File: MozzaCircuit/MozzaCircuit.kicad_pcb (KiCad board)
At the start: 2 copper layers, 11 parts

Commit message: init pcb
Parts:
- removed C?: C_2012, 00_KeyParts:C_2012
- removed L? (x2): WS2812B, 00_KeyParts:WS2812B_2020_rev
- removed REF** (x3): ChocV2_rev, 00_KeyParts:ChocV2_rev
- removed REF** (x3): C_0603_1608Metric_Pad1.08x0.95mm_HandSolder, Capacitor_SMD:C_0603_1608Metric_Pad1.08x0.95mm_HandSolder
- removed REF**: D_SOD-323_HandSoldering, Diode_SMD:D_SOD-323_HandSoldering
- removed REF**: WS2812C-2020, 00_KeyParts:LED_WS2812C-2020_BackMount_v2
- added C1: 0.1u, 00_KeyParts:C_2012, F.Cu at (206.2, 46.5)
- added C11: 0.1u, 00_KeyParts:C_2012_rev, F.Cu at (59.6, 141.2)
- added C12: C_Small, 00_KeyParts:C_2012_rev, F.Cu at (74.7, 130.1)
- added C13: C_Small, 00_KeyParts:C_2012_rev, F.Cu at (64.3, 144.2)
- added C14: C_Small, 00_KeyParts:C_2012_rev, F.Cu at (64.8, 138.3)
- added C15: C_Small, 00_KeyParts:C_2012_rev, F.Cu at (54.8, 142.4)
- added C2: C_Small, 00_KeyParts:C_2012, F.Cu at (234.0, 28.9)
- added C21: C_Small, 00_KeyParts:C_2012_rev, F.Cu at (44.4, 151.8)
- added C22: C_Small, 00_KeyParts:C_2012_rev, F.Cu at (69.5, 134.2)
- added C23: C_Small, 00_KeyParts:C_2012_rev, F.Cu at (59.6, 144.2)
- added C24: C_Small, 00_KeyParts:C_2012_rev, F.Cu at (74.3, 136.0)
- added C25: C_Small, 00_KeyParts:C_2012_rev, F.Cu at (49.6, 150.7)
- added C31: C_Small, 00_KeyParts:C_2012_rev, F.Cu at (64.8, 135.3)
- added C32: C_Small, 00_KeyParts:C_2012_rev, F.Cu at (54.4, 148.3)
- added C33: C_Small, 00_KeyParts:C_2012_rev, F.Cu at (53.9, 154.2)
- added C34: C_Small, 00_KeyParts:C_2012_rev, F.Cu at (70.4, 127.1)
- added C35: C_Small, 00_KeyParts:C_2012_rev, F.Cu at (64.3, 141.2)
- added C41: C_Small, 00_KeyParts:C_2012_rev, F.Cu at (69.5, 140.1)
- added C42: C_Small, 00_KeyParts:C_2012_rev, F.Cu at (54.8, 139.5)
- added C43: C_Small, 00_KeyParts:C_2012_rev, F.Cu at (79.9, 127.1)
- added C44: C_Small, 00_KeyParts:C_2012_rev, F.Cu at (59.6, 147.1)
- added C51: C_Small, 00_KeyParts:C_2012_rev, F.Cu at (64.3, 147.1)
- added C52: C_Small, 00_KeyParts:C_2012_rev, F.Cu at (49.6, 147.7)
- added C53: C_Small, 00_KeyParts:C_2012_rev, F.Cu at (79.5, 130.1)
- added C54: C_Small, 00_KeyParts:C_2012_rev, F.Cu at (69.5, 137.1)
- added C61: C_Small, 00_KeyParts:C_2012_rev, F.Cu at (49.2, 153.6)
- added C62: C_Small, 00_KeyParts:C_2012_rev, F.Cu at (70.0, 131.2)
- added C63: C_Small, 00_KeyParts:C_2012_rev, F.Cu at (75.2, 127.1)
- added C64: C_Small, 00_KeyParts:C_2012_rev, F.Cu at (60.0, 135.3)
- added C71: C_Small, 00_KeyParts:C_2012_rev, F.Cu at (59.1, 150.1)
- added C72: C_Small, 00_KeyParts:C_2012_rev, F.Cu at (74.7, 133.0)
- added C73: C_Small, 00_KeyParts:C_2012_rev, F.Cu at (65.2, 131.2)
- added C82: C_Small, 00_KeyParts:C_2012_rev, F.Cu at (54.8, 145.4)
- added C83: C_Small, 00_KeyParts:C_2012_rev, F.Cu at (60.0, 138.3)
- added C84: C_Small, 00_KeyParts:C_2012_rev, F.Cu at (54.4, 151.3)
- added CA1: 33n, 00_KeyParts:C_2012_rev, F.Cu at (159.7, 58.7)
- added CB1: C_Small, 00_KeyParts:C_2012_rev, F.Cu at (178.2, 34.8)
- added CD1: 33n, 00_KeyParts:C_2012_rev, F.Cu at (174.6, 49.8)
- added CD2: C_Small, 00_KeyParts:C_2012_rev, F.Cu at (164.7, 52.8)
- added CD3: C_Small, 00_KeyParts:C_2012_rev, F.Cu at (183.0, 37.8)
- added CD4: C_Small, 00_KeyParts:C_2012_rev, F.Cu at (99.5, 118.7)
- added CD5: C_Small, 00_KeyParts:C_2012_rev, F.Cu at (178.2, 43.7)
- added CD6: C_Small, 00_KeyParts:C_2012_rev, F.Cu at (141.7, 76.6)
- added CD7: C_Small, 00_KeyParts:C_2012_rev, F.Cu at (159.7, 64.6)
- added CD8: C_Small, 00_KeyParts:C_2012_rev, F.Cu at (94.8, 118.7)
- added D12: D_Small, 00_KeyParts:D_SOD-323_both_sides, F.Cu at (141.9, 67.8)
- added D13: D_Small, 00_KeyParts:D_SOD-323_both_sides, F.Cu at (147.0, 67.8)
- added D15: D_Small, 00_KeyParts:D_SOD-323_both_sides, F.Cu at (64.6, 118.7)
- added D21: D_Small, 00_KeyParts:D_SOD-323_both_sides, F.Cu at (89.9, 118.7)
- added D22: D_Small, 00_KeyParts:D_SOD-323_both_sides, F.Cu at (39.3, 118.7)
- added D23: D_Small, 00_KeyParts:D_SOD-323_both_sides, F.Cu at (170.0, 46.9)
- added D24: D_Small, 00_KeyParts:D_SOD-323_both_sides, F.Cu at (59.5, 118.7)
- added D25: D_Small, 00_KeyParts:D_SOD-323_both_sides, F.Cu at (69.6, 118.7)
- added D31: D_Small, 00_KeyParts:D_SOD-323_both_sides, F.Cu at (164.9, 46.9)
- added D32: D_Small, 00_KeyParts:D_SOD-323_both_sides, F.Cu at (44.3, 116.8)
- added D33: D_Small, 00_KeyParts:D_SOD-323_both_sides, F.Cu at (159.9, 46.9)
- added D34: D_Small, 00_KeyParts:D_SOD-323_both_sides, F.Cu at (147.0, 64.8)
- added D35: D_Small, 00_KeyParts:D_SOD-323_both_sides, F.Cu at (159.9, 49.8)
- added D41: D_Small, 00_KeyParts:D_SOD-323_both_sides, F.Cu at (178.4, 31.9)
- added D42: D_Small, 00_KeyParts:D_SOD-323_both_sides, F.Cu at (74.7, 118.7)
- added D43: D_Small, 00_KeyParts:D_SOD-323_both_sides, F.Cu at (164.9, 49.8)
- added D44: D_Small, 00_KeyParts:D_SOD-323_both_sides, F.Cu at (141.9, 70.7)
- added D45: D_Small, 00_KeyParts:D_SOD-323_both_sides, F.Cu at (152.0, 64.8)
- added D51: D_Small, 00_KeyParts:D_SOD-323_both_sides, F.Cu at (159.9, 55.7)
- added D52: D_Small, 00_KeyParts:D_SOD-323_both_sides, F.Cu at (34.2, 119.7)
- added D53: D_Small, 00_KeyParts:D_SOD-323_both_sides, F.Cu at (44.3, 119.7)
- added D54: D_Small, 00_KeyParts:D_SOD-323_both_sides, F.Cu at (159.9, 52.8)
- added D61: D_Small, 00_KeyParts:D_SOD-323_both_sides, F.Cu at (183.5, 28.9)
- added D62: D_Small, 00_KeyParts:D_SOD-323_both_sides, F.Cu at (141.9, 73.7)
- added D63: D_Small, 00_KeyParts:D_SOD-323_both_sides, F.Cu at (79.7, 118.7)
- added D64: D_Small, 00_KeyParts:D_SOD-323_both_sides, F.Cu at (178.4, 28.9)
- added D71: D_Small, 00_KeyParts:D_SOD-323_both_sides, F.Cu at (141.9, 64.8)
- added D72: D_Small, 00_KeyParts:D_SOD-323_both_sides, F.Cu at (54.4, 118.7)
- added D73: D_Small, 00_KeyParts:D_SOD-323_both_sides, F.Cu at (34.2, 116.8)
- added D82: D_Small, 00_KeyParts:D_SOD-323_both_sides, F.Cu at (84.8, 118.7)
- added D83: D_Small, 00_KeyParts:D_SOD-323_both_sides, F.Cu at (49.4, 118.7)
- added D84: D_Small, 00_KeyParts:D_SOD-323_both_sides, F.Cu at (124.0, 100.7)
- added J1: 8P8C_both_sides, 00_KeyParts:RJ45_Molex_0955032884_both_sides, F.Cu at (213.4, 30.0)
- added JPB2: SolderJumper_2_Open, Jumper:SolderJumper-2_P1.3mm_Open_TrianglePad1.0x1.5mm, F.Cu at (238.2, 32.8)
- added JPB3: SolderJumper_2_Open, Jumper:SolderJumper-2_P1.3mm_Open_TrianglePad1.0x1.5mm, F.Cu at (242.5, 32.8)
- added JPB4: SolderJumper_2_Open, Jumper:SolderJumper-2_P1.3mm_Open_TrianglePad1.0x1.5mm, F.Cu at (233.8, 32.2)
- added JPB6: SolderJumper_2_Open, Jumper:SolderJumper-2_P1.3mm_Open_TrianglePad1.0x1.5mm, F.Cu at (242.9, 29.2)
- added JPB7: SolderJumper_2_Open, Jumper:SolderJumper-2_P1.3mm_Open_TrianglePad1.0x1.5mm, F.Cu at (225.1, 46.7)
- added JPB8: SolderJumper_2_Open, Jumper:SolderJumper-2_P1.3mm_Open_TrianglePad1.0x1.5mm, F.Cu at (238.6, 29.2)
- added JPF2: SolderJumper_2_Open, Jumper:SolderJumper-2_P1.3mm_Open_TrianglePad1.0x1.5mm, F.Cu at (233.8, 39.3)
- added JPF3: SolderJumper_2_Open, Jumper:SolderJumper-2_P1.3mm_Open_TrianglePad1.0x1.5mm, F.Cu at (215.1, 46.8)
- added JPF4: SolderJumper_2_Open, Jumper:SolderJumper-2_P1.3mm_Open_TrianglePad1.0x1.5mm, F.Cu at (238.2, 36.3)
- added JPF6: SolderJumper_2_Open, Jumper:SolderJumper-2_P1.3mm_Open_TrianglePad1.0x1.5mm, F.Cu at (233.8, 35.7)
- added JPF7: SolderJumper_2_Open, Jumper:SolderJumper-2_P1.3mm_Open_TrianglePad1.0x1.5mm, F.Cu at (210.8, 46.8)
- added JPF8: SolderJumper_2_Open, Jumper:SolderJumper-2_P1.3mm_Open_TrianglePad1.0x1.5mm, F.Cu at (219.5, 46.8)
- added L12: WS2812-2020_both_sides, 00_KeyParts:WS2812B_2020_rev, F.Cu at (55.1, 135.9)
- added L13: WS2812-2020_both_sides, 00_KeyParts:WS2812B_2020_rev, F.Cu at (44.7, 144.2)
- added L15: WS2812-2020_both_sides, 00_KeyParts:WS2812B_2020_rev, F.Cu at (44.7, 131.8)
- added L21: WS2812-2020_both_sides, 00_KeyParts:WS2812B_2020_rev, F.Cu at (49.9, 140.0)
- added L22: WS2812-2020_both_sides, 00_KeyParts:WS2812B_2020_rev, F.Cu at (60.3, 131.8)
- added L23: WS2812-2020_both_sides, 00_KeyParts:WS2812B_2020_rev, F.Cu at (39.5, 148.3)
- added L24: WS2812-2020_both_sides, 00_KeyParts:WS2812B_2020_rev, F.Cu at (44.7, 127.7)
- added L25: WS2812-2020_both_sides, 00_KeyParts:WS2812B_2020_rev, F.Cu at (60.3, 127.7)
- added L31: WS2812-2020_both_sides, 00_KeyParts:WS2812B_2020_rev, F.Cu at (44.7, 148.3)
- added L32: WS2812-2020_both_sides, 00_KeyParts:WS2812B_2020_rev, F.Cu at (49.9, 131.8)
- added L33: WS2812-2020_both_sides, 00_KeyParts:WS2812B_2020_rev, F.Cu at (39.5, 144.2)
- added L34: WS2812-2020_both_sides, 00_KeyParts:WS2812B_2020_rev, F.Cu at (34.3, 127.7)
- added L35: WS2812-2020_both_sides, 00_KeyParts:WS2812B_2020_rev, F.Cu at (39.5, 135.9)
- added L41: WS2812-2020_both_sides, 00_KeyParts:WS2812B_2020_rev, F.Cu at (39.5, 140.0)
- added L42: WS2812-2020_both_sides, 00_KeyParts:WS2812B_2020_rev, F.Cu at (65.5, 127.7)
- added L43: WS2812-2020_both_sides, 00_KeyParts:WS2812B_2020_rev, F.Cu at (39.5, 131.8)
- added L44: WS2812-2020_both_sides, 00_KeyParts:WS2812B_2020_rev, F.Cu at (49.9, 135.9)
- added L51: WS2812-2020_both_sides, 00_KeyParts:WS2812B_2020_rev, F.Cu at (34.3, 140.0)
- added L52: WS2812-2020_both_sides, 00_KeyParts:WS2812B_2020_rev, F.Cu at (55.1, 131.8)
- added L53: WS2812-2020_both_sides, 00_KeyParts:WS2812B_2020_rev, F.Cu at (39.5, 152.4)
- added L54: WS2812-2020_both_sides, 00_KeyParts:WS2812B_2020_rev, F.Cu at (39.5, 127.7)
- added L61: WS2812-2020_both_sides, 00_KeyParts:WS2812B_2020_rev, F.Cu at (34.3, 152.4)
- added L62: WS2812-2020_both_sides, 00_KeyParts:WS2812B_2020_rev, F.Cu at (34.3, 135.9)
- added L63: WS2812-2020_both_sides, 00_KeyParts:WS2812B_2020_rev, F.Cu at (44.7, 140.0)
- added L64: WS2812-2020_both_sides, 00_KeyParts:WS2812B_2020_rev, F.Cu at (49.9, 144.2)
- added L71: WS2812-2020_both_sides, 00_KeyParts:WS2812B_2020_rev, F.Cu at (49.9, 127.7)
- added L72: WS2812-2020_both_sides, 00_KeyParts:WS2812B_2020_rev, F.Cu at (34.3, 148.3)
- added L73: WS2812-2020_both_sides, 00_KeyParts:WS2812B_2020_rev, F.Cu at (55.1, 127.7)
- added L82: WS2812-2020_both_sides, 00_KeyParts:WS2812B_2020_rev, F.Cu at (34.3, 144.2)
- added L83: WS2812-2020_both_sides, 00_KeyParts:WS2812B_2020_rev, F.Cu at (34.3, 131.8)
- added L84: WS2812-2020_both_sides, 00_KeyParts:WS2812B_2020_rev, F.Cu at (44.7, 135.9)
- added R11: 10k, 00_KeyParts:R_2012_rev, F.Cu at (104.3, 118.7)
- added R12: 4k7, 00_KeyParts:R_2012_rev, F.Cu at (188.0, 31.9)
- added R21: R_Small_US, 00_KeyParts:R_2012_rev, F.Cu at (146.8, 73.7)
- added R22: R_Small_US, 00_KeyParts:R_2012_rev, F.Cu at (146.8, 70.7)
- added R31: R_Small_US, 00_KeyParts:R_2012_rev, F.Cu at (169.8, 49.8)
- added R32: R_Small_US, 00_KeyParts:R_2012_rev, F.Cu at (188.4, 28.9)
- added R41: R_Small_US, 00_KeyParts:R_2012_rev, F.Cu at (159.7, 61.6)
- added R42: R_Small_US, 00_KeyParts:R_2012_rev, F.Cu at (178.2, 37.8)
- added R51: R_Small_US, 00_KeyParts:R_2012_rev, F.Cu at (183.3, 31.9)
- added R52: R_Small_US, 00_KeyParts:R_2012_rev, F.Cu at (164.7, 55.7)
- added R61: R_Small_US, 00_KeyParts:R_2012_rev, F.Cu at (164.4, 58.7)
- added R62: R_Small_US, 00_KeyParts:R_2012_rev, F.Cu at (183.0, 34.8)
- added R71: R_Small_US, 00_KeyParts:R_2012_rev, F.Cu at (146.5, 76.6)
- added R72: R_Small_US, 00_KeyParts:R_2012_rev, F.Cu at (151.5, 70.7)
- added R81: R_Small_US, 00_KeyParts:R_2012_rev, F.Cu at (174.9, 46.9)
- added R82: R_Small_US, 00_KeyParts:R_2012_rev, F.Cu at (169.5, 52.8)
- added RA1: 10k, 00_KeyParts:R_2012_rev, F.Cu at (187.7, 34.8)
- added RA2: 4k7, 00_KeyParts:R_2012_rev, F.Cu at (178.2, 40.7)
- added RB1: R_Small_US, 00_KeyParts:R_2012_rev, F.Cu at (193.1, 28.9)
- added RB2: R_Small_US, 00_KeyParts:R_2012_rev, F.Cu at (183.0, 40.7)
- added RE1: RotaryEncoder_Switch, 00_KeyParts:RotaryEncoder_Bourns_PEC12R-4215F, F.Cu at (41.2, 35.5)
- added SW12: SW_ChocV2_rev, 00_KeyParts:ChocV2_rev, F.Cu at (113.0, 36.4)
- added SW13: SW_ChocV2_rev, 00_KeyParts:ChocV2_rev, F.Cu at (76.5, 108.2)
- added SW15: SW_ChocV2_rev, 00_KeyParts:ChocV2_rev, F.Cu at (40.6, 106.3)
- added SW21: SW_ChocV2_rev, 00_KeyParts:ChocV2_rev, F.Cu at (58.6, 72.3)
- added SW22: SW_ChocV2_rev, 00_KeyParts:ChocV2_rev, F.Cu at (59.2, 36.4)
- added SW23: SW_ChocV2_rev, 00_KeyParts:ChocV2_rev, F.Cu at (130.4, 72.3)
- added SW24: SW_ChocV2_rev, 00_KeyParts:ChocV2_rev, F.Cu at (40.6, 52.5)
- added SW25: SW_ChocV2_rev, 00_KeyParts:ChocV2_rev, F.Cu at (77.1, 36.4)
- added SW31: SW_ChocV2_rev, 00_KeyParts:ChocV2_rev, F.Cu at (148.9, 36.4)
- added SW32: SW_ChocV2_rev, 00_KeyParts:ChocV2_rev, F.Cu at (112.4, 72.3)
- added SW33: SW_ChocV2_rev, 00_KeyParts:ChocV2_rev, F.Cu at (76.5, 90.3)
- added SW34: SW_ChocV2_rev, 00_KeyParts:ChocV2_rev, F.Cu at (112.4, 54.4)
- added SW35: SW_ChocV2_rev, 00_KeyParts:ChocV2_rev, F.Cu at (94.5, 72.3)
- added SW41: SW_ChocV2_rev, 00_KeyParts:ChocV2_rev, F.Cu at (166.9, 36.4)
- added SW42: SW_ChocV2_rev, 00_KeyParts:ChocV2_rev, F.Cu at (40.6, 70.4)
- added SW43: SW_ChocV2_rev, 00_KeyParts:ChocV2_rev, F.Cu at (130.4, 90.3)
- added SW44: SW_ChocV2_rev, 00_KeyParts:ChocV2_rev, F.Cu at (94.5, 90.3)
- added SW51: SW_ChocV2_rev, 00_KeyParts:ChocV2_rev, F.Cu at (76.5, 54.4)
- added SW52: SW_ChocV2_rev, 00_KeyParts:ChocV2_rev, F.Cu at (131.0, 36.4)
- added SW53: SW_ChocV2_rev, 00_KeyParts:ChocV2_rev, F.Cu at (130.4, 54.4)
- added SW54: SW_ChocV2_rev, 00_KeyParts:ChocV2_rev, F.Cu at (94.5, 54.4)
- added SW61: SW_ChocV2_rev, 00_KeyParts:ChocV2_rev, F.Cu at (58.6, 108.2)
- added SW62: SW_ChocV2_rev, 00_KeyParts:ChocV2_rev, F.Cu at (76.5, 72.3)
- added SW63: SW_ChocV2_rev, 00_KeyParts:ChocV2_rev, F.Cu at (94.5, 108.2)
- added SW64: SW_ChocV2_rev, 00_KeyParts:ChocV2_rev, F.Cu at (58.6, 90.3)
- added SW71: SW_ChocV2_rev, 00_KeyParts:ChocV2_rev, F.Cu at (95.1, 36.4)
- added SW72: SW_ChocV2_rev, 00_KeyParts:ChocV2_rev, F.Cu at (40.6, 88.4)
- added SW73: SW_ChocV2_rev, 00_KeyParts:ChocV2_rev, F.Cu at (148.3, 54.4)
- added SW82: SW_ChocV2_rev, 00_KeyParts:ChocV2_rev, F.Cu at (58.6, 54.4)
- added SW83: SW_ChocV2_rev, 00_KeyParts:ChocV2_rev, F.Cu at (112.4, 90.3)
- added SW84: SW_ChocV2_rev, 00_KeyParts:ChocV2_rev, F.Cu at (112.4, 108.2)
- added U1: MCP23017_ML, 00_KeyParts:QFN-28-1EP_6x6mm_P0.65mm_EP4.25x4.25mm_Hand, F.Cu at (227.3, 40.6)
- added U2: MCP23017_ML, 00_KeyParts:QFN-28-1EP_6x6mm_P0.65mm_EP4.25x4.25mm_Hand_NoTP, F.Cu at (227.3, 31.8)
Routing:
- net (no net): track 96.9 -> 0.00 mm, vias 8 -> 0

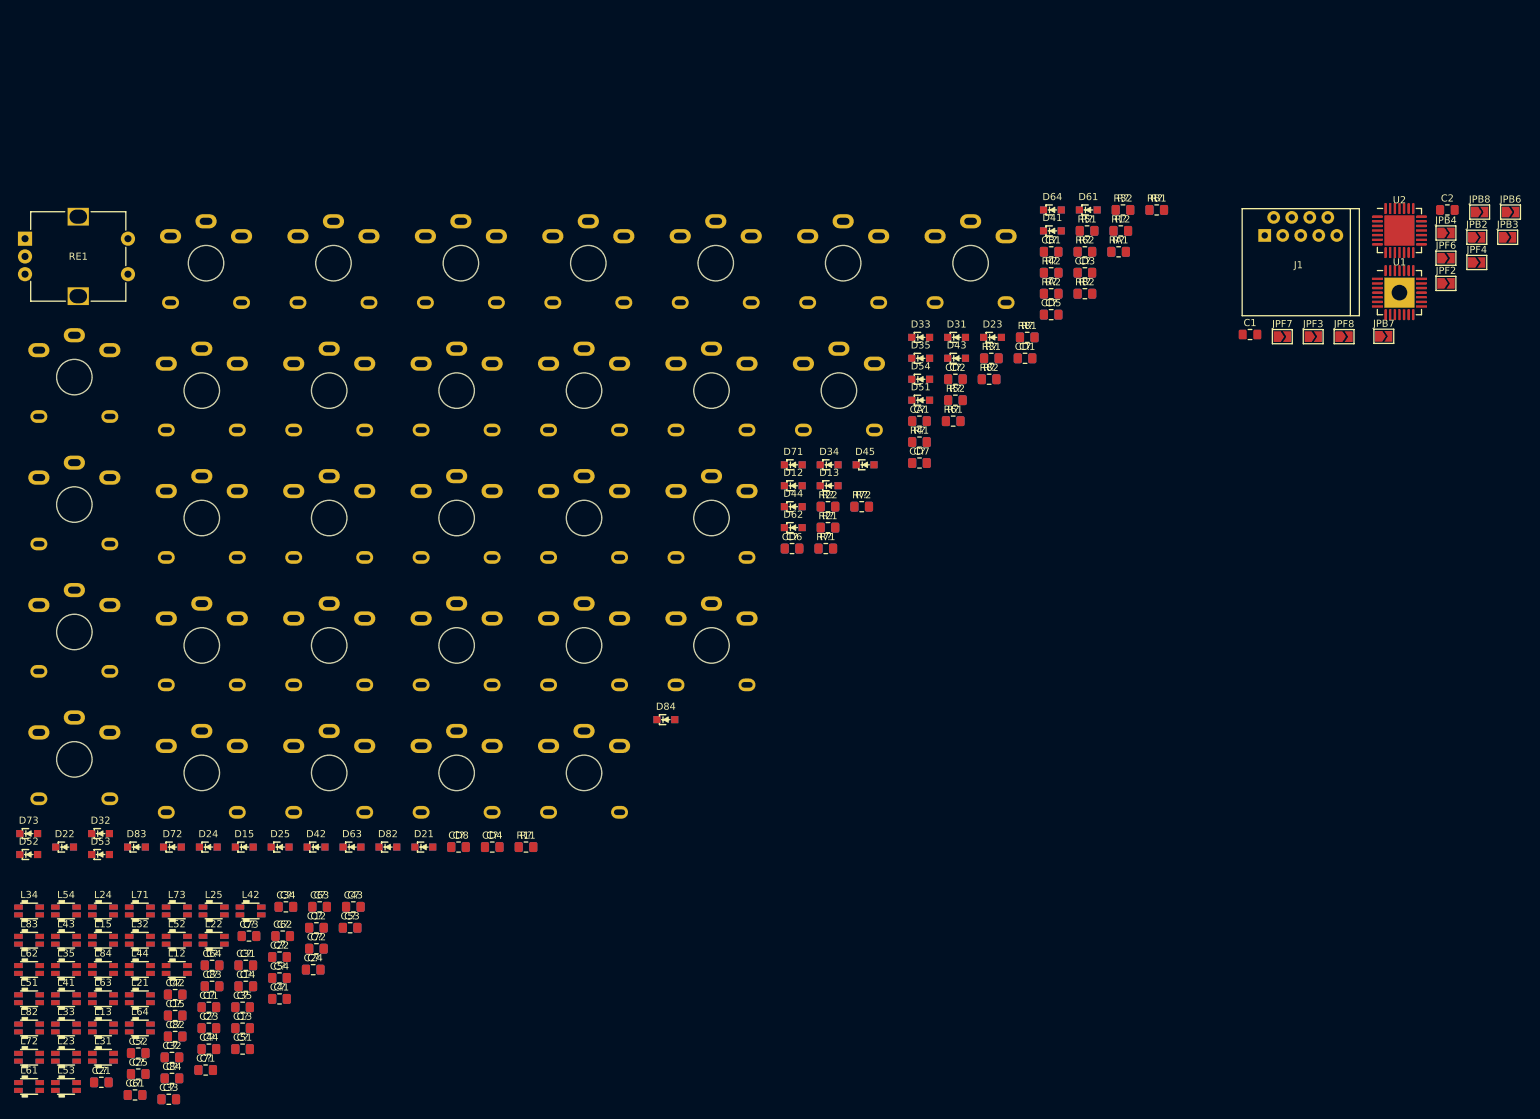
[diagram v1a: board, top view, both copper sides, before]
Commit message: placed sw and led
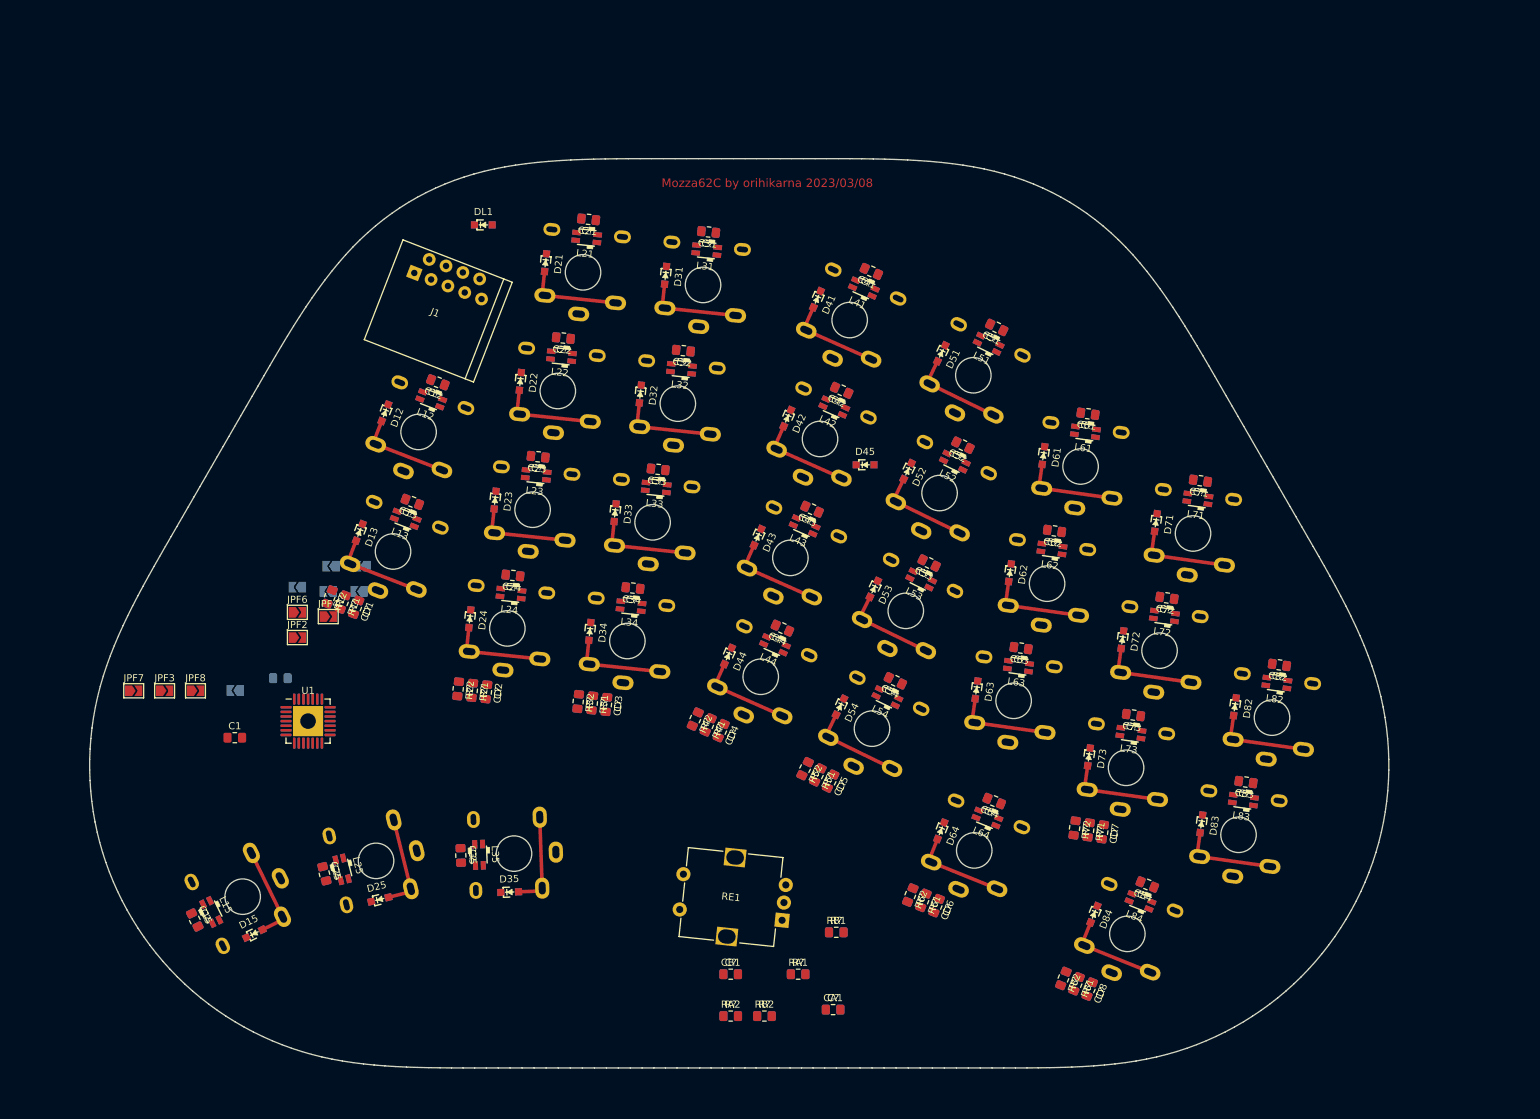
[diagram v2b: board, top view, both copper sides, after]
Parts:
- removed C11: 0.1u, 00_KeyParts:C_2012_rev
- removed C14: C_Small, 00_KeyParts:C_2012_rev
- added DL1: D_Small, 00_KeyParts:D_SOD-323_both_sides, F.Cu at (98.2, 31.0)
- C2, JPB2, JPB3, JPB4, JPB6, JPB7, JPB8: moved to B.Cu
- C21: value C_Small -> 0.1u
- U2: value MCP23017_ML -> MCP23017_ML_NoTP; moved to B.Cu
- moved L82 182.4 mm to (210.0, 95.6), turned to 172 degrees
- moved C2 177.1 mm to (69.7, 94.9), turned to 180 degrees
- moved L61 175.1 mm to (183.1, 60.2), turned to 172 degrees
- moved L83 172.2 mm to (205.3, 112.1), turned to 172 degrees
- moved L72 171.6 mm to (194.2, 86.1), turned to 172 degrees
- moved JPB2 169.3 mm to (76.4, 82.7), turned to 180 degrees
- moved JPB3 169.3 mm to (80.8, 82.7), turned to 180 degrees
- moved JPB4 169.3 mm to (72.0, 82.1), turned to 180 degrees
- moved JPB6 169.3 mm to (81.2, 79.1), turned to 180 degrees
- moved JPB7 169.3 mm to (63.3, 96.6), turned to 180 degrees
- moved JPB8 169.3 mm to (76.8, 79.1), turned to 180 degrees
- moved JPF2 169.3 mm to (72.0, 89.2)
- moved JPF3 169.3 mm to (53.4, 96.7)
- moved JPF4 169.3 mm to (76.4, 86.2)
- moved JPF6 169.3 mm to (72.0, 85.6)
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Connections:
- L21 pad 4: 5VD -> 4V3D
- SW12 pad 3: 5VD -> Net-(D12-Pad2)
- SW12 pad 4: GNDD -> 5VD
- SW13 pad 3: 5VD -> Net-(D13-Pad2)
- SW13 pad 4: GNDD -> 5VD
- SW15 pad 3: GNDD -> ROW5
- SW15 pad 4: 5VD -> GNDD
- SW21 pad 3: 5VD -> Net-(D21-Pad2)
- SW21 pad 4: GNDD -> 5VD
- SW22 pad 3: 5VD -> Net-(D22-Pad2)
- SW22 pad 4: GNDD -> 5VD
- SW23 pad 3: 5VD -> Net-(D23-Pad2)
- SW23 pad 4: GNDD -> 5VD
- SW24 pad 3: 5VD -> Net-(D24-Pad2)
- SW24 pad 4: GNDD -> 5VD
- SW25 pad 3: 5VD -> Net-(D25-Pad2)
- SW25 pad 4: GNDD -> 5VD
- SW31 pad 3: 5VD -> Net-(D31-Pad2)
- SW31 pad 4: GNDD -> 5VD
- SW32 pad 3: 5VD -> Net-(D32-Pad2)
- SW32 pad 4: GNDD -> 5VD
- SW33 pad 3: 5VD -> Net-(D33-Pad2)
- SW33 pad 4: GNDD -> 5VD
- SW34 pad 3: 5VD -> Net-(D34-Pad2)
- SW34 pad 4: GNDD -> 5VD
- SW35 pad 3: 5VD -> Net-(D35-Pad2)
- SW35 pad 4: GNDD -> 5VD
- SW41 pad 3: 5VD -> Net-(D41-Pad2)
- SW41 pad 4: GNDD -> 5VD
- SW42 pad 3: 5VD -> Net-(D42-Pad2)
- SW42 pad 4: GNDD -> 5VD
- SW43 pad 3: 5VD -> Net-(D43-Pad2)
- SW43 pad 4: GNDD -> 5VD
- SW44 pad 3: 5VD -> Net-(D44-Pad2)
- SW44 pad 4: GNDD -> 5VD
- SW51 pad 3: 5VD -> Net-(D51-Pad2)
- SW51 pad 4: GNDD -> 5VD
- SW52 pad 3: 5VD -> Net-(D52-Pad2)
- SW52 pad 4: GNDD -> 5VD
- SW53 pad 3: 5VD -> Net-(D53-Pad2)
- SW53 pad 4: GNDD -> 5VD
- SW54 pad 3: 5VD -> Net-(D54-Pad2)
- SW54 pad 4: GNDD -> 5VD
- SW61 pad 3: 5VD -> Net-(D61-Pad2)
- SW61 pad 4: GNDD -> 5VD
- SW62 pad 3: 5VD -> Net-(D62-Pad2)
- SW62 pad 4: GNDD -> 5VD
- SW63 pad 3: 5VD -> Net-(D63-Pad2)
- SW63 pad 4: GNDD -> 5VD
- SW64 pad 3: 5VD -> Net-(D64-Pad2)
- SW64 pad 4: GNDD -> 5VD
- SW71 pad 3: 5VD -> Net-(D71-Pad2)
- SW71 pad 4: GNDD -> 5VD
- SW72 pad 3: 5VD -> Net-(D72-Pad2)
- SW72 pad 4: GNDD -> 5VD
- SW73 pad 3: 5VD -> Net-(D73-Pad2)
- SW73 pad 4: GNDD -> 5VD
- SW82 pad 3: 5VD -> Net-(D82-Pad2)
- SW82 pad 4: GNDD -> 5VD
- SW83 pad 3: 5VD -> Net-(D83-Pad2)
- SW83 pad 4: GNDD -> 5VD
- SW84 pad 3: 5VD -> Net-(D84-Pad2)
- SW84 pad 4: GNDD -> 5VD
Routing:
- net Net-(D12-Pad2): track 0.00 -> 13.8 mm
- net Net-(D13-Pad2): track 0.00 -> 13.8 mm
- net Net-(D35-Pad2): track 0.00 -> 13.8 mm
- net Net-(D33-Pad2): track 0.00 -> 13.8 mm
- net Net-(D22-Pad2): track 0.00 -> 13.8 mm
- net Net-(D21-Pad2): track 0.00 -> 13.8 mm
- net Net-(D32-Pad2): track 0.00 -> 13.8 mm
- net Net-(D31-Pad2): track 0.00 -> 13.8 mm
- net Net-(D34-Pad2): track 0.00 -> 13.8 mm
- net Net-(D24-Pad2): track 0.00 -> 13.8 mm
- net Net-(D23-Pad2): track 0.00 -> 13.8 mm
- net Net-(D43-Pad2): track 0.00 -> 13.7 mm
- net Net-(D41-Pad2): track 0.00 -> 13.7 mm
- net Net-(D44-Pad2): track 0.00 -> 13.7 mm
- net Net-(D42-Pad2): track 0.00 -> 13.7 mm
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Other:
- board outline added: 183 x 128.1 mm
- board text added: "Mozza62C by orihikarna 2023/03/08"

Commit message: led direction
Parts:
- moved D45 67.1 mm to (121.5, 124.6)
- moved C13 17.2 mm to (91.8, 53.2)
- moved C14 17.2 mm to (88.2, 70.1)
- moved CD1 17.2 mm to (83.9, 68.1)
- moved D13 17.2 mm to (84.4, 57.5)
- moved D14 17.2 mm to (80.8, 74.3)
- moved R11 17.2 mm to (82.1, 67.3)
- moved R12 17.2 mm to (80.2, 66.6)
- moved SW13 17.2 mm to (89.1, 60.2)
- moved SW14 17.2 mm to (85.5, 77.0)
- moved L13 17.2 mm to (90.9, 55.6)
- moved L14 17.2 mm to (87.3, 72.4), turned to -21.2 degrees
- moved D35 10.8 mm to (101.6, 114.2)
- moved D25 10.8 mm to (81.1, 115.6)
- moved D15 10.8 mm to (61.3, 121.2)
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- renumbered C12 to C14, D12 to D14, L12 to L14, SW12 to SW14
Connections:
- L13 pad 3: Net-(L12-Pad1) -> Net-(L13-Pad3)
- L13 pad 7: Net-(L12-Pad1) -> Net-(L13-Pad3)
- L14 pad 1: Net-(L12-Pad1) -> Net-(L14-Pad1)
- L14 pad 3: Net-(L12-Pad3) -> Net-(L14-Pad3)
- L14 pad 5: Net-(L12-Pad1) -> Net-(L14-Pad1)
- L14 pad 7: Net-(L12-Pad3) -> Net-(L14-Pad3)
- L15 pad 3: Net-(L15-Pad3) -> Net-(L14-Pad1)
- L15 pad 7: Net-(L15-Pad3) -> Net-(L14-Pad1)
- L22 pad 1: Net-(L12-Pad3) -> Net-(L13-Pad3)
- L22 pad 5: Net-(L12-Pad3) -> Net-(L13-Pad3)
- L24 pad 1: Net-(L15-Pad3) -> Net-(L14-Pad3)
- L24 pad 5: Net-(L15-Pad3) -> Net-(L14-Pad3)
- SW14 pad 1: ROW2 -> ROW4
- SW14 pad 4: 5VD -> unconnected-(SW14-Pad4)
- SW14 pad 5: GNDD -> unconnected-(SW14-Pad5)
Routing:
- net ROW3: track 0.00 -> 147.5 mm
- net ROW4: track 0.00 -> 130.2 mm
- net ROW2: track 0.00 -> 124.6 mm
- net ROW1: track 0.00 -> 103.3 mm
- net Net-(D25-Pad2): track 13.7 -> 17.5 mm
- net Net-(D13-Pad2): track 13.8 -> 17.5 mm
- net Net-(D14-Pad2): track 13.8 -> 17.5 mm
- net Net-(D22-Pad2): track 13.8 -> 17.5 mm
- net Net-(D21-Pad2): track 13.8 -> 17.5 mm
- net Net-(D33-Pad2): track 13.8 -> 17.5 mm
- net Net-(D32-Pad2): track 13.8 -> 17.5 mm
- net Net-(D31-Pad2): track 13.8 -> 17.5 mm
- net Net-(D24-Pad2): track 13.8 -> 17.5 mm
- net Net-(D23-Pad2): track 13.8 -> 17.5 mm
- net Net-(D34-Pad2): track 13.8 -> 17.5 mm
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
